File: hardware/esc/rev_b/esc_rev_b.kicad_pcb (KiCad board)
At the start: 4 copper layers, 196 x 296 mm, 646 parts, among them J1101 FUSED_BATTERY_TAP, J1102 MOTOR_PHASES, J1103 LOCAL_SWD, J1201 FUSED_BATTERY_TAP, J1202 MOTOR_PHASES, J1203 LOCAL_SWD, J1301 FUSED_BATTERY_TAP, J1302 MOTOR_PHASES, J1303 LOCAL_SWD, J1401 FUSED_BATTERY_TAP, J1402 MOTOR_PHASES, J1403 LOCAL_SWD, J1501 FUSED_BATTERY_TAP, J1502 MOTOR_PHASES, J1503 LOCAL_SWD, J1601 FUSED_BATTERY_TAP, J1602 MOTOR_PHASES, J1603 LOCAL_SWD, J201 ESC_SWD, J701 AUX_BATTERY, J702 FLIGHT_CAN_POWER, Q1101 IPTC014N10NM5, Q1102 IPTC014N10NM5, Q1103 IPTC014N10NM5, Q1104 IPTC014N10NM5, Q1105 IPTC014N10NM5, Q1106 IPTC014N10NM5, Q1201 IPTC014N10NM5, Q1202 IPTC014N10NM5, Q1203 IPTC014N10NM5, Q1204 IPTC014N10NM5, Q1205 IPTC014N10NM5, Q1206 IPTC014N10NM5, Q1301 IPTC014N10NM5, Q1302 IPTC014N10NM5, Q1303 IPTC014N10NM5, Q1304 IPTC014N10NM5, Q1305 IPTC014N10NM5, Q1306 IPTC014N10NM5, Q1401 IPTC014N10NM5, Q1402 IPTC014N10NM5, Q1403 IPTC014N10NM5, Q1404 IPTC014N10NM5, Q1405 IPTC014N10NM5, Q1406 IPTC014N10NM5, Q1501 IPTC014N10NM5, Q1502 IPTC014N10NM5, Q1503 IPTC014N10NM5, Q1504 IPTC014N10NM5, Q1505 IPTC014N10NM5, Q1506 IPTC014N10NM5, Q1601 IPTC014N10NM5, Q1602 IPTC014N10NM5, Q1603 IPTC014N10NM5, Q1604 IPTC014N10NM5, Q1605 IPTC014N10NM5, Q1606 IPTC014N10NM5, U1101 DRV8353SRTAR, U1102 STM32G431CBT6, U1103 ISO6731FDWR, U1104 TPS70933DBVR, U1105 INA296A2IDR, U1106 SN74LVC1G08DBVR, U1201 DRV8353SRTAR, U1202 STM32G431CBT6, U1203 ISO6731FDWR, U1204 TPS70933DBVR, U1205 INA296A2IDR, U1206 SN74LVC1G08DBVR, U1301 DRV8353SRTAR, U1302 STM32G431CBT6, U1303 ISO6731FDWR, U1304 TPS70933DBVR, U1305 INA296A2IDR, U1306 SN74LVC1G08DBVR, U1401 DRV8353SRTAR, U1402 STM32G431CBT6, U1403 ISO6731FDWR, U1404 TPS70933DBVR, U1405 INA296A2IDR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

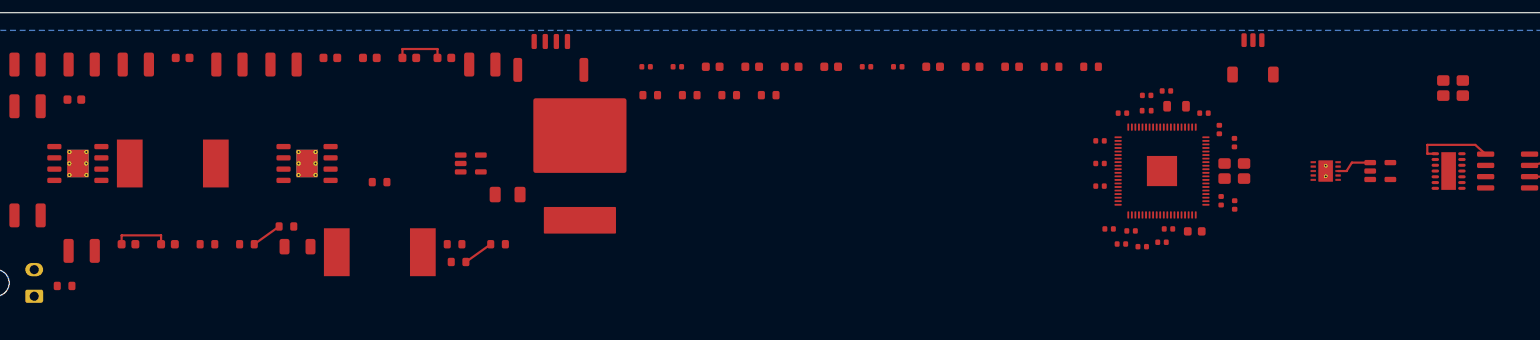
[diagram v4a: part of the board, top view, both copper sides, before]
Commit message: esc: hand route ten more signal links
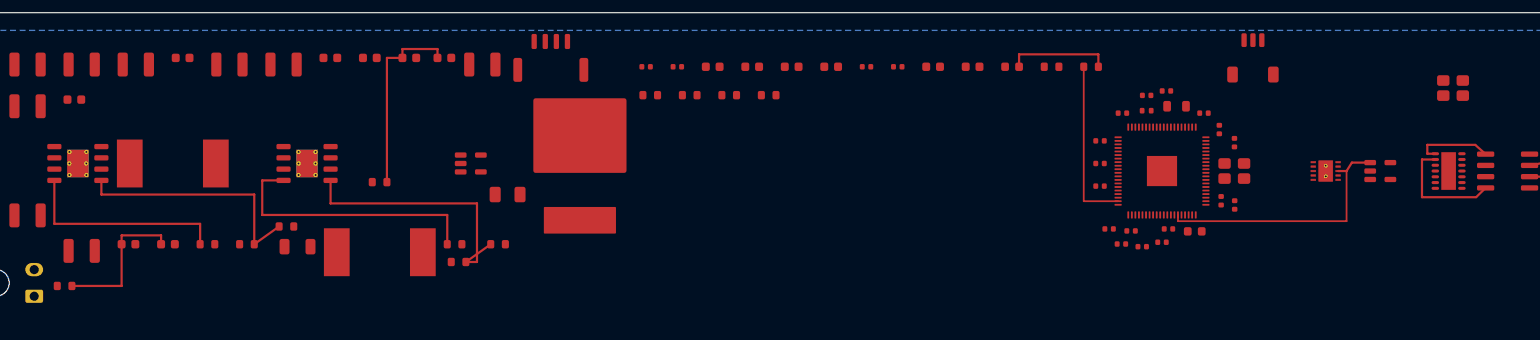
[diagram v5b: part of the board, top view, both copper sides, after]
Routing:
- net /Auxiliary power/LM2_RON: track 0.00 -> 30.4 mm
- net /Auxiliary power/LM2_FB: track 3.44 -> 30.4 mm
- net /Controller and ADC/ESC_RUN: track 4.14 -> 29.5 mm
- net /Auxiliary power/LM_FB: track 3.44 -> 27.9 mm
- net /Auxiliary power/LM_RON: track 0.00 -> 23.6 mm
- net /Controller and ADC/STATUS_LED: track 0.00 -> 19.0 mm
- net /Auxiliary power/LM_RIPPLE: track 5.95 -> 21.7 mm
- net /Controller and ADC/U207_RXCAN: track 0.00 -> 13.3 mm
- net /Controller and ADC/ESC_LED_A: track 0.00 -> 11.7 mm
- net /Auxiliary power/LM2_RIPPLE: track 6.45 -> 16.8 mm
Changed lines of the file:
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@@
+	)
+	(segment
+		(start 62.2 21.5)
+		(end 62.2 28.1)
+		(width 0.25)
+		(layer "F.Cu")
+		(net 9)
+	)
+	(segment
+		(start 62.2 28.1)
+		(end 60.95 28.1)
+		(width 0.25)
+		(layer "F.Cu")
+		(net 9)
+	)
+	(segment
+		(start 45.7 21.5)
+		(end 62.2 21.5)
+		(width 0.25)
+		(layer "F.Cu")
+		(net 9)
 	)
 	(segment
@@
 	)
 	(segment
+		(start 45.7 18.905)
+		(end 45.7 21.5)
+		(width 0.25)
+		(layer "F.Cu")
+		(net 9)
+	)
+	(segment
+		(start 22.15 30.8)
+		(end 22.15 26.1)
+		(width 0.25)
+		(layer "F.Cu")
+		(net 10)
+	)
+	(segment
+		(start 16.55 30.8)
+		(end 22.15 30.8)
+		(width 0.25)
+		(layer "F.Cu")
+		(net 10)
+	)
+	(segment
 		(start 22.15 25.1)
 		(end 26.6 25.1)
@@
 	)
 	(segment
+		(start 38 22.8)
+		(end 58.85 22.8)
+		(width 0.25)
+		(layer "F.Cu")
+		(net 11)
+	)
+	(segment
+		(start 38 18.905)
+		(end 38 22.8)
+		(width 0.25)
+		(layer "F.Cu")
+		(net 11)
+	)
+	(segment
+		(start 40.4 18.905)
+		(end 38 18.905)
+		(width 0.25)
+		(layer "F.Cu")
+		(net 11)
+	)
+	(segment
+		(start 58.85 22.8)
+		(end 58.85 26.1)
+		(width 0.25)
+		(layer "F.Cu")
+		(net 11)
+	)
+	(segment
+		(start 37.1 20.5)
+		(end 37.1 26.1)
+		(width 0.25)
+		(layer "F.Cu")
+		(net 14)
+	)
+	(segment
 		(start 37.1 26.1)
 		(end 39.9 24.1)
@@
 	)
 	(segment
+		(start 19.87 20.5)
+		(end 37.1 20.5)
+		(width 0.25)
+		(layer "F.Cu")
+		(net 14)
+	)
+	(segment
+		(start 19.87 18.905)
+		(end 19.87 20.5)
+		(width 0.25)
+		(layer "F.Cu")
+		(net 14)
+	)
+	(segment
+		(start 52.05 5.1)
+		(end 53.8 5.1)
+		(width 0.25)
+		(layer "F.Cu")
+		(net 15)
+	)
+	(segment
 		(start 53.8 4.099999)
 		(end 57.75 4.099999)
@@
 		(layer "F.Cu")
 		(net 15)
+	)
+	(segment
+		(start 52.05 19.1)
+		(end 52.05 5.1)
+		(width 0.25)
+		(layer "F.Cu")
+		(net 15)
+	)
+	(segment
+		(start 31 23.8)
+		(end 31 26.1)
+		(width 0.25)
+		(layer "F.Cu")
+		(net 16)
+	)
+	(segment
+		(start 14.57 18.905)
+		(end 14.57 23.8)
+		(width 0.25)
+		(layer "F.Cu")
+		(net 16)
+	)
+	(segment
+		(start 14.57 23.8)
+		(end 31 23.8)
+		(width 0.25)
+		(layer "F.Cu")
+		(net 16)
 	)
 	(segment
@@
 	)
 	(segment
+		(start 123.2925 6.1)
+		(end 123.2925 4.7)
+		(width 0.25)
+		(layer "F.Cu")
+		(net 28)
+	)
+	(segment
+		(start 123.2925 4.7)
+		(end 132.229999 4.7)
+		(width 0.25)
+		(layer "F.Cu")
+		(net 28)
+	)
+	(segment
+		(start 132.229999 4.7)
+		(end 132.23 6.1)
+		(width 0.25)
+		(layer "F.Cu")
+		(net 28)
+	)
+	(segment
 		(start 159.25 17.849999)
 		(end 160.2 17.85)
@@
 	)
 	(segment
+		(start 141.2 23.5)
+		(end 160.2 23.5)
+		(width 0.2)
+		(layer "F.Cu")
+		(net 29)
+	)
+	(segment
+		(start 141.2 22.799999)
+		(end 141.2 23.5)
+		(width 0.2)
+		(layer "F.Cu")
+		(net 29)
+	)
+	(segment
+		(start 160.2 23.5)
+		(end 160.2 17.85)
+		(width 0.2)
+		(layer "F.Cu")
+		(net 29)
+	)
+	(segment
 		(start 160.8 16.9)
 		(end 162.8625 16.899999)
@@
 	)
 	(segment
+		(start 130.58 6.1)
+		(end 130.58 21.25)
+		(width 0.2)
+		(layer "F.Cu")
+		(net 32)
+	)
+	(segment
+		(start 130.58 21.25)
+		(end 134.45 21.249999)
+		(width 0.2)
+		(layer "F.Cu")
+		(net 32)
+	)
+	(segment
 		(start 180.825 17.214999)
 		(end 183.495 16.724999)
@@
 	)
 	(segment
+		(start 174.8 20.8)
+		(end 175.875 19.754999)
+		(width 0.25)
+		(layer "F.Cu")
+		(net 39)
+	)
+	(segment
+		(start 168.7 20.8)
+		(end 174.8 20.8)
+		(width 0.25)
+		(layer "F.Cu")
+		(net 39)
+	)
+	(segment
+		(start 170.2 16.549999)
+		(end 168.7 16.55)
+		(width 0.25)
+		(layer "F.Cu")
+		(net 39)
+	)
+	(segment
+		(start 168.7 16.55)
+		(end 168.7 20.8)
+		(width 0.25)
+		(layer "F.Cu")
+		(net 39)
+	)
+	(segment
